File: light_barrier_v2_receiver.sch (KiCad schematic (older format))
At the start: 25 parts, among them J1 POWER, Q1 BC557, Q2 TIP120, U1 VS1838, U2 TLC555CP, U3 TLC555CP

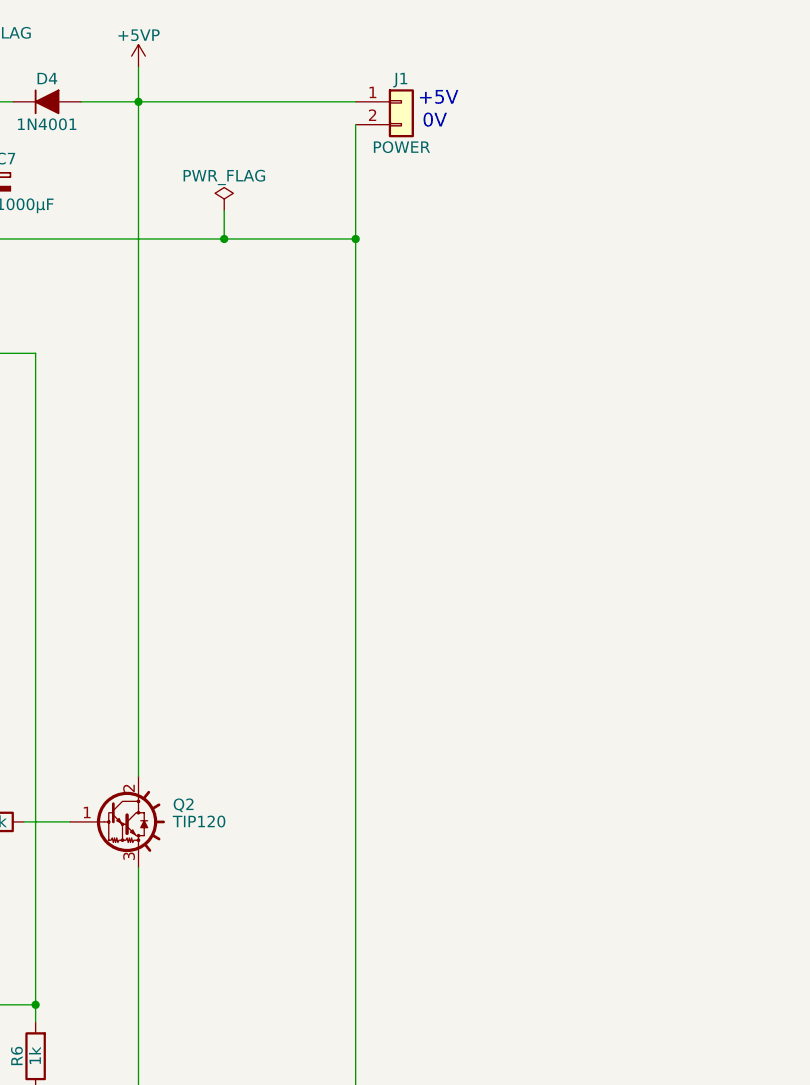
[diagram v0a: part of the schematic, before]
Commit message: Added warning to schematics
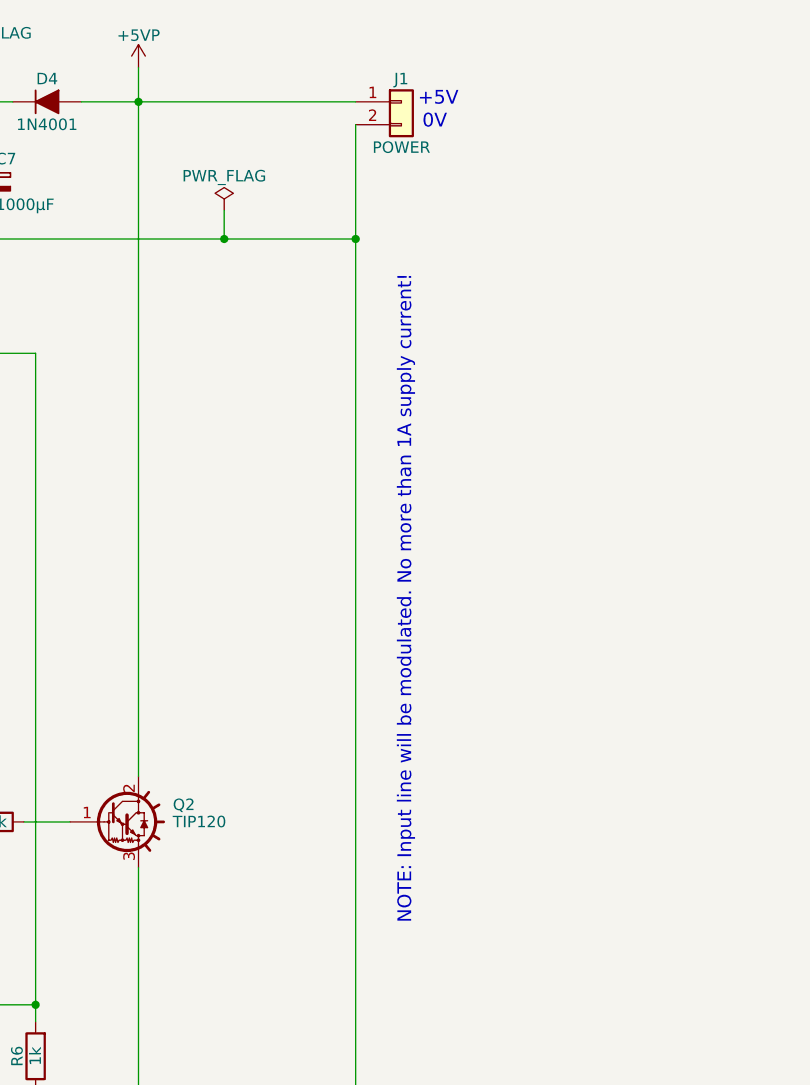
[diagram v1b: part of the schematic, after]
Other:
- note added: "NOTE: Input line will be modulated. No more than 1A supply current!"
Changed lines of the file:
@@
 	1    0    0    -1
 $EndComp
+Text Notes 6950 5200 1    60   ~ 0
+NOTE: Input line will be modulated. No more than 1A supply current!
 $EndSCHEMATC
